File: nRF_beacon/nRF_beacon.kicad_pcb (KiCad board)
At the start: 4 copper layers, 100 x 60 mm, 59 parts, among them J1 Conn_02x05_Odd_Even, J2 Conn_02x03_Counter_Clockwise, U1 nRF54L15-QFAA, U2 NPM1300-QEAA-R7, U3 MAX98357A, U4 12BHC186P1-GR, X1 32MHz, X2 32.768 kHz

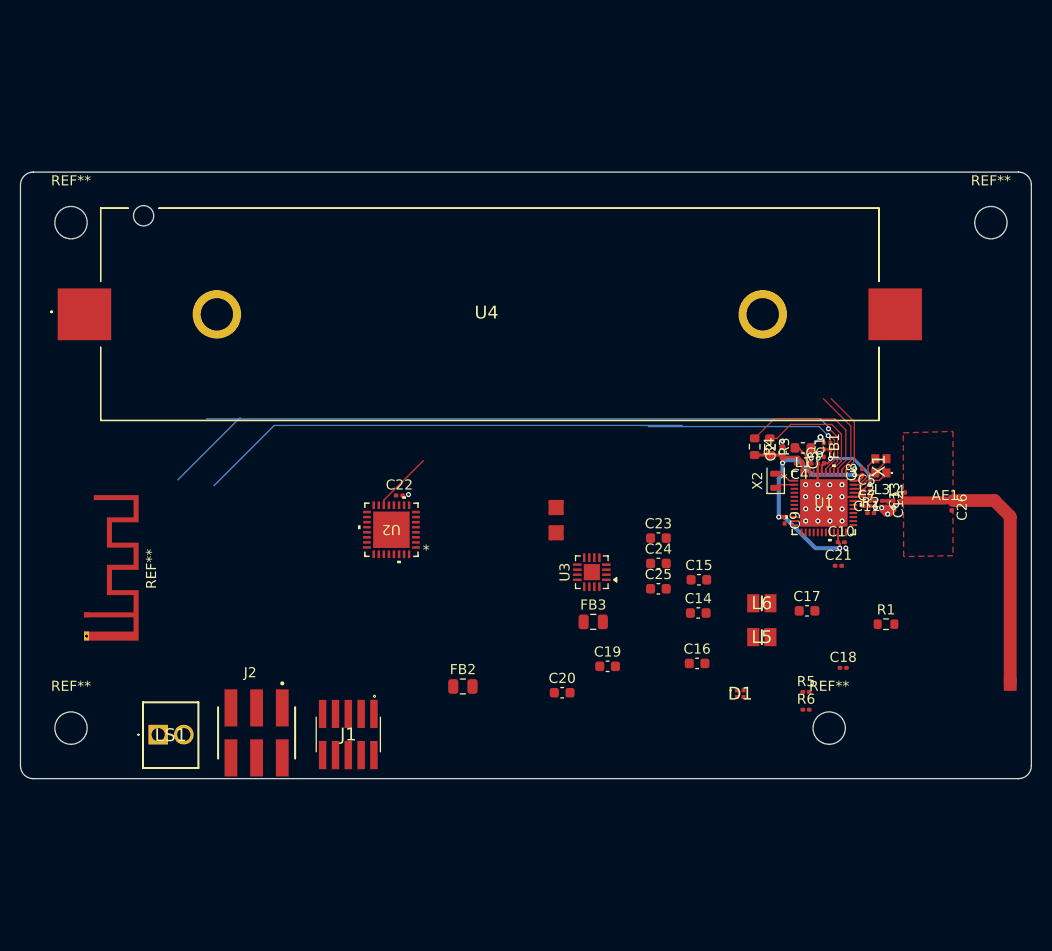
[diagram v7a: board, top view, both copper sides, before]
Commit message: Began typical application around nPM1300
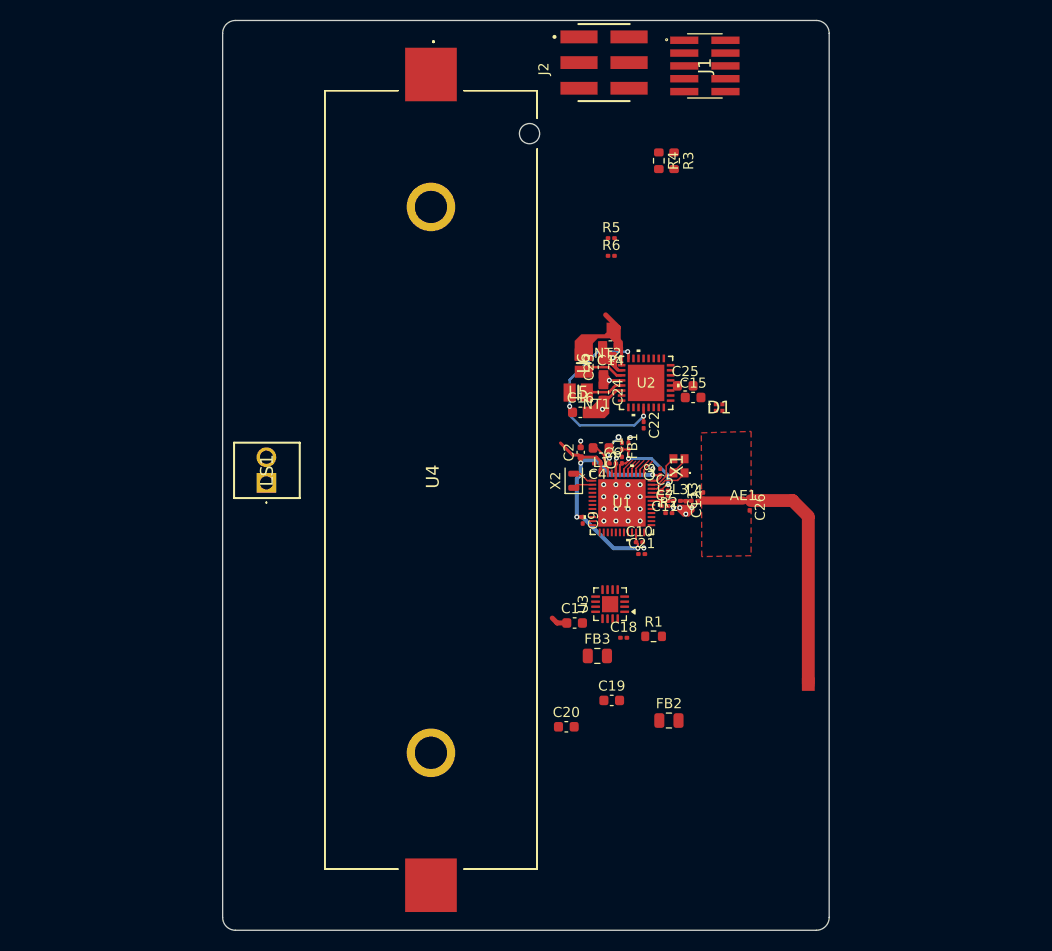
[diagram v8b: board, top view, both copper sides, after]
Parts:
- removed REF** (x4): MountingHole_3.2mm_M3, MountingHole:MountingHole_3.2mm_M3
- removed REF**: Texas_SWRA117D_2.4GHz_Left, RF_Antenna:Texas_SWRA117D_2.4GHz_Left
- NT1, NT2: footprint NetTie:NetTie-4_SMD_Pad0.5mm -> Ekse:NetTieSmall
- moved J1 75.0 mm to (167.7, 59.5), turned to -90 degrees
- moved J2 74.7 mm to (157.7, 59.2), turned to 90 degrees
- moved R5 48.9 mm to (158.4, 76.5)
- moved R6 48.9 mm to (158.4, 78.3)
- moved L5 30.3 mm to (155.2, 91.8), turned to 0 degrees
- moved R3 29.8 mm to (164.7, 68.9)
- moved R4 29.8 mm to (163.1, 68.9)
- moved L6 29.6 mm to (155.7, 88.9), turned to -90 degrees
- moved U2 29.1 mm to (161.9, 90.9), turned to 0 degrees
- moved D1 28.4 mm to (169.1, 93.3)
- moved C14 27.8 mm to (158.4, 87.2), turned to 180 degrees
- moved C16 27.4 mm to (155.4, 93.8)
- moved LS1 27.1 mm to (124.3, 100.7), turned to 90 degrees
- moved C22 25.2 mm to (161.6, 95.0), turned to -90 degrees
- moved C17 23.0 mm to (154.8, 114.6)
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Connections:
- C14 pad 2: Net-(U2-PVSS1) -> VSS1
- C16 pad 2: Net-(U2-PVSS2) -> VSS2
- C23 pad 2: Net-(C23-Pad2) -> VSS1
- C24 pad 2: Net-(C24-Pad2) -> VSS2
- NT1 pad 1: Net-(U2-PVSS2) -> VSS2
- NT2 pad 1: Net-(U2-PVSS1) -> VSS1
- U2 pad 2: Net-(U2-PVSS1) -> VSS1
- U2 pad 6: Net-(U2-PVSS2) -> VSS2
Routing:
- net /P1.13: track 75.6 -> 1.53 mm, vias 1 -> 0
- net /P1.14: track 71.4 -> 1.66 mm, vias 1 -> 0
- net VDD_nRF: track 32.3 -> 53.4 mm, vias 4 -> 7
- net /MCU/SCL: track 18.5 -> 1.55 mm
- net /MCU/SDA: track 14.9 -> 1.60 mm
- net VDD_AUDIO: track 0.00 -> 7.57 mm
- net /P1.10: track 8.87 -> 1.64 mm
- net /P1.09: track 8.69 -> 1.54 mm
- net /POWER/SW2: track 0.00 -> 3.73 mm
- net /POWER/SW1: track 0.00 -> 3.40 mm
- net Net-(U2-PVDD): track 0.00 -> 1.15 mm, vias 0 -> 1
- net GND: track 11.4 -> 12.0 mm, vias 25 -> 27
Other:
- board size 100 x 60 mm -> 60 x 90 mm
